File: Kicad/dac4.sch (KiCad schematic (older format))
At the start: 10 parts

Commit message: Add 4-bit Video DAC, and re-wire BMC.
Now the BMC is an SPI device, and has a four-wire UART.
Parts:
- renumbered R105 to R1401, R106 to R1402, R107 to R1403, R108 to R1404, R109 to R1405, R110 to R1406, R111 to R1407, R112 to R1408, R113 to R1409, R114 to R1410
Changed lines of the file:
@@
 Sheet 14 16
 Title "Neotron Common Hardware - 4-bit DAC"
-Date "2021-01-01"
+Date "2021-04-02"
 Rev "[Uncontrolled]"
 Comp "https://neotron-compute.github.io/"
@@
 AR Path="/5FDE658D/6009CBAC/5F5F4D05" Ref="R?"  Part="1"
 AR Path="/5FDE658D/600A04B7/5F5F4D05" Ref="R?"  Part="1"
-AR Path="/60677AF0/5FEFB226/5F5F4D05" Ref="R105"  Part="1"
-AR Path="/60677AF0/6068202E/5F5F4D05" Ref="R115"  Part="1"
-AR Path="/60677AF0/600A04B7/5F5F4D05" Ref="R125"  Part="1"
-F 0 "R125" H 3570 2746 50  0000 L CNN
+AR Path="/60677AF0/5FEFB226/5F5F4D05" Ref="R1401"  Part="1"
+AR Path="/60677AF0/6068202E/5F5F4D05" Ref="R1501"  Part="1"
+AR Path="/60677AF0/600A04B7/5F5F4D05" Ref="R1601"  Part="1"
+F 0 "R1601" H 3570 2746 50  0000 L CNN
 F 1 "24k 0.5%" H 3570 2655 50  0000 L CNN
 F 2 "Resistor_SMD:R_0805_2012Metric_Pad1.20x1.40mm_HandSolder" V 3430 2700 50  0001 C CNN
@@
 AR Path="/5FDE658D/6009CBAC/60681FF9" Ref="R?"  Part="1"
 AR Path="/5FDE658D/600A04B7/60681FF9" Ref="R?"  Part="1"
-AR Path="/60677AF0/5FEFB226/60681FF9" Ref="R107"  Part="1"
-AR Path="/60677AF0/6068202E/60681FF9" Ref="R117"  Part="1"
-AR Path="/60677AF0/600A04B7/60681FF9" Ref="R127"  Part="1"
-F 0 "R127" V 4100 3000 50  0000 C CNN
+AR Path="/60677AF0/5FEFB226/60681FF9" Ref="R1403"  Part="1"
+AR Path="/60677AF0/6068202E/60681FF9" Ref="R1503"  Part="1"
+AR Path="/60677AF0/600A04B7/60681FF9" Ref="R1603"  Part="1"
+F 0 "R1603" V 4100 3000 50  0000 C CNN
 F 1 "12k 0.5%" V 4200 3000 50  0000 C CNN
 F 2 "Resistor_SMD:R_0805_2012Metric_Pad1.20x1.40mm_HandSolder" V 3930 3000 50  0001 C CNN
@@
 AR Path="/5FDE658D/6009CBAC/60681FFA" Ref="R?"  Part="1"
 AR Path="/5FDE658D/600A04B7/60681FFA" Ref="R?"  Part="1"
-AR Path="/60677AF0/5FEFB226/60681FFA" Ref="R108"  Part="1"
-AR Path="/60677AF0/6068202E/60681FFA" Ref="R118"  Part="1"
-AR Path="/60677AF0/600A04B7/60681FFA" Ref="R128"  Part="1"
-F 0 "R128" H 4570 2746 50  0000 L CNN
+AR Path="/60677AF0/5FEFB226/60681FFA" Ref="R1404"  Part="1"
+AR Path="/60677AF0/6068202E/60681FFA" Ref="R1504"  Part="1"
+AR Path="/60677AF0/600A04B7/60681FFA" Ref="R1604"  Part="1"
+F 0 "R1604" H 4570 2746 50  0000 L CNN
 F 1 "24k 0.5%" H 4570 2655 50  0000 L CNN
 F 2 "Resistor_SMD:R_0805_2012Metric_Pad1.20x1.40mm_HandSolder" V 4430 2700 50  0001 C CNN
@@
 AR Path="/5FDE658D/6009CBAC/60681FFB" Ref="R?"  Part="1"
 AR Path="/5FDE658D/600A04B7/60681FFB" Ref="R?"  Part="1"
-AR Path="/60677AF0/5FEFB226/60681FFB" Ref="R109"  Part="1"
-AR Path="/60677AF0/6068202E/60681FFB" Ref="R119"  Part="1"
-AR Path="/60677AF0/600A04B7/60681FFB" Ref="R129"  Part="1"
-F 0 "R129" V 5100 3000 50  0000 C CNN
+AR Path="/60677AF0/5FEFB226/60681FFB" Ref="R1405"  Part="1"
+AR Path="/60677AF0/6068202E/60681FFB" Ref="R1505"  Part="1"
+AR Path="/60677AF0/600A04B7/60681FFB" Ref="R1605"  Part="1"
+F 0 "R1605" V 5100 3000 50  0000 C CNN
 F 1 "12k 0.5%" V 5200 3000 50  0000 C CNN
 F 2 "Resistor_SMD:R_0805_2012Metric_Pad1.20x1.40mm_HandSolder" V 4930 3000 50  0001 C CNN
@@
 AR Path="/5FDE658D/6009CBAC/60681FFC" Ref="R?"  Part="1"
 AR Path="/5FDE658D/600A04B7/60681FFC" Ref="R?"  Part="1"
-AR Path="/60677AF0/5FEFB226/60681FFC" Ref="R111"  Part="1"
-AR Path="/60677AF0/6068202E/60681FFC" Ref="R121"  Part="1"
-AR Path="/60677AF0/600A04B7/60681FFC" Ref="R131"  Part="1"
-F 0 "R131" V 6100 3000 50  0000 C CNN
+AR Path="/60677AF0/5FEFB226/60681FFC" Ref="R1407"  Part="1"
+AR Path="/60677AF0/6068202E/60681FFC" Ref="R1507"  Part="1"
+AR Path="/60677AF0/600A04B7/60681FFC" Ref="R1607"  Part="1"
+F 0 "R1607" V 6100 3000 50  0000 C CNN
 F 1 "12k 0.5%" V 6200 3000 50  0000 C CNN
 F 2 "Resistor_SMD:R_0805_2012Metric_Pad1.20x1.40mm_HandSolder" V 5930 3000 50  0001 C CNN
@@
 AR Path="/5FDE658D/6009CBAC/60681FFD" Ref="R?"  Part="1"
 AR Path="/5FDE658D/600A04B7/60681FFD" Ref="R?"  Part="1"
-AR Path="/60677AF0/5FEFB226/60681FFD" Ref="R113"  Part="1"
-AR Path="/60677AF0/6068202E/60681FFD" Ref="R123"  Part="1"
-AR Path="/60677AF0/600A04B7/60681FFD" Ref="R133"  Part="1"
-F 0 "R133" V 7100 3000 50  0000 C CNN
+AR Path="/60677AF0/5FEFB226/60681FFD" Ref="R1409"  Part="1"
+AR Path="/60677AF0/6068202E/60681FFD" Ref="R1509"  Part="1"
+AR Path="/60677AF0/600A04B7/60681FFD" Ref="R1609"  Part="1"
+F 0 "R1609" V 7100 3000 50  0000 C CNN
 F 1 "12k 0.5%" V 7200 3000 50  0000 C CNN
 F 2 "Resistor_SMD:R_0805_2012Metric_Pad1.20x1.40mm_HandSolder" V 6930 3000 50  0001 C CNN
@@
 AR Path="/5FDE658D/6009CBAC/60681FFF" Ref="R?"  Part="1"
 AR Path="/5FDE658D/600A04B7/60681FFF" Ref="R?"  Part="1"
-AR Path="/60677AF0/5FEFB226/60681FFF" Ref="R114"  Part="1"
-AR Path="/60677AF0/6068202E/60681FFF" Ref="R124"  Part="1"
-AR Path="/60677AF0/600A04B7/60681FFF" Ref="R134"  Part="1"
-F 0 "R134" H 7620 3346 50  0000 L CNN
+AR Path="/60677AF0/5FEFB226/60681FFF" Ref="R1410"  Part="1"
+AR Path="/60677AF0/6068202E/60681FFF" Ref="R1510"  Part="1"
+AR Path="/60677AF0/600A04B7/60681FFF" Ref="R1610"  Part="1"
+F 0 "R1610" H 7620 3346 50  0000 L CNN
 F 1 "3480 0.5%" H 7620 3255 50  0000 L CNN
 F 2 "Resistor_SMD:R_0805_2012Metric_Pad1.20x1.40mm_HandSolder" V 7480 3300 50  0001 C CNN
@@
 AR Path="/5FDE658D/6009CBAC/60682000" Ref="#PWR?"  Part="1"
 AR Path="/5FDE658D/600A04B7/60682000" Ref="#PWR?"  Part="1"
-AR Path="/60677AF0/5FEFB226/60682000" Ref="#PWR0224"  Part="1"
-AR Path="/60677AF0/6068202E/60682000" Ref="#PWR0226"  Part="1"
-AR Path="/60677AF0/600A04B7/60682000" Ref="#PWR0228"  Part="1"
-F 0 "#PWR0228" H 3500 3350 50  0001 C CNN
+AR Path="/60677AF0/5FEFB226/60682000" Ref="#PWR01401"  Part="1"
+AR Path="/60677AF0/6068202E/60682000" Ref="#PWR01501"  Part="1"
+AR Path="/60677AF0/600A04B7/60682000" Ref="#PWR01601"  Part="1"
+F 0 "#PWR01601" H 3500 3350 50  0001 C CNN
 F 1 "GND" H 3505 3427 50  0000 C CNN
 F 2 "" H 3500 3600 50  0001 C CNN
@@
 AR Path="/5FDE658D/6009CBAC/60682001" Ref="#PWR?"  Part="1"
 AR Path="/5FDE658D/600A04B7/60682001" Ref="#PWR?"  Part="1"
-AR Path="/60677AF0/5FEFB226/60682001" Ref="#PWR0225"  Part="1"
-AR Path="/60677AF0/6068202E/60682001" Ref="#PWR0227"  Part="1"
-AR Path="/60677AF0/600A04B7/60682001" Ref="#PWR0229"  Part="1"
-F 0 "#PWR0229" H 7550 3350 50  0001 C CNN
+AR Path="/60677AF0/5FEFB226/60682001" Ref="#PWR01402"  Part="1"
+AR Path="/60677AF0/6068202E/60682001" Ref="#PWR01502"  Part="1"
+AR Path="/60677AF0/600A04B7/60682001" Ref="#PWR01602"  Part="1"
+F 0 "#PWR01602" H 7550 3350 50  0001 C CNN
 F 1 "GND" H 7555 3427 50  0000 C CNN
 F 2 "" H 7550 3600 50  0001 C CNN
@@
 AR Path="/5FDE658D/6009CBAC/60682002" Ref="R?"  Part="1"
 AR Path="/5FDE658D/600A04B7/60682002" Ref="R?"  Part="1"
-AR Path="/60677AF0/5FEFB226/60682002" Ref="R106"  Part="1"
-AR Path="/60677AF0/6068202E/60682002" Ref="R116"  Part="1"
-AR Path="/60677AF0/600A04B7/60682002" Ref="R126"  Part="1"
-F 0 "R126" H 3570 3346 50  0000 L CNN
+AR Path="/60677AF0/5FEFB226/60682002" Ref="R1402"  Part="1"
+AR Path="/60677AF0/6068202E/60682002" Ref="R1502"  Part="1"
+AR Path="/60677AF0/600A04B7/60682002" Ref="R1602"  Part="1"
+F 0 "R1602" H 3570 3346 50  0000 L CNN
 F 1 "24k 0.5%" H 3570 3255 50  0000 L CNN
 F 2 "Resistor_SMD:R_0805_2012Metric_Pad1.20x1.40mm_HandSolder" V 3430 3300 50  0001 C CNN
@@
 AR Path="/5FDE658D/6009CBAC/60682003" Ref="R?"  Part="1"
 AR Path="/5FDE658D/600A04B7/60682003" Ref="R?"  Part="1"
-AR Path="/60677AF0/5FEFB226/60682003" Ref="R110"  Part="1"
-AR Path="/60677AF0/6068202E/60682003" Ref="R120"  Part="1"
-AR Path="/60677AF0/600A04B7/60682003" Ref="R130"  Part="1"
-F 0 "R130" H 5570 2746 50  0000 L CNN
+AR Path="/60677AF0/5FEFB226/60682003" Ref="R1406"  Part="1"
+AR Path="/60677AF0/6068202E/60682003" Ref="R1506"  Part="1"
+AR Path="/60677AF0/600A04B7/60682003" Ref="R1606"  Part="1"
+F 0 "R1606" H 5570 2746 50  0000 L CNN
 F 1 "24k 0.5%" H 5570 2655 50  0000 L CNN
 F 2 "Resistor_SMD:R_0805_2012Metric_Pad1.20x1.40mm_HandSolder" V 5430 2700 50  0001 C CNN
@@
 AR Path="/5FDE658D/6009CBAC/5F5FD329" Ref="R?"  Part="1"
 AR Path="/5FDE658D/600A04B7/5F5FD329" Ref="R?"  Part="1"
-AR Path="/60677AF0/5FEFB226/5F5FD329" Ref="R112"  Part="1"
-AR Path="/60677AF0/6068202E/5F5FD329" Ref="R122"  Part="1"
-AR Path="/60677AF0/600A04B7/5F5FD329" Ref="R132"  Part="1"
-F 0 "R132" H 6570 2746 50  0000 L CNN
+AR Path="/60677AF0/5FEFB226/5F5FD329" Ref="R1408"  Part="1"
+AR Path="/60677AF0/6068202E/5F5FD329" Ref="R1508"  Part="1"
+AR Path="/60677AF0/600A04B7/5F5FD329" Ref="R1608"  Part="1"
+F 0 "R1608" H 6570 2746 50  0000 L CNN
 F 1 "24k 0.5%" H 6570 2655 50  0000 L CNN
 F 2 "Resistor_SMD:R_0805_2012Metric_Pad1.20x1.40mm_HandSolder" V 6430 2700 50  0001 C CNN

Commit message: Tidy up part nos and swapped I2C/UART on BMC.
Mark all resistors as 1% if not specified.
Added some Mouser part numbers.
BMC can now be programmed over UART.
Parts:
- R1410: Digikey RMCF0805FG3K30-ND -> RNCF0805DTE3K48CT-ND; MPN RMCF0805FG3K30 -> RNCF0805DTE3K48
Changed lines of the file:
@@
 F 3 "~" H 7550 3300 50  0001 C CNN
 F 4 "0" H 7550 3300 50  0001 C CNN "DNP"
-F 5 "RMCF0805FG3K30-ND" H 7550 3300 50  0001 C CNN "Digikey"
-F 6 "RMCF0805FG3K30" H 7550 3300 50  0001 C CNN "MPN"
+F 5 "RNCF0805DTE3K48CT-ND" H 7550 3300 50  0001 C CNN "Digikey"
+F 6 "RNCF0805DTE3K48" H 7550 3300 50  0001 C CNN "MPN"
 F 7 "Stackpole" H 7550 3300 50  0001 C CNN "Manufacturer"
 	1    7550 3300

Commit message: Changes to BMC
* Swapped BUTTON_PWR and SYS_RESET to avoid DRC issue
* Split PSU and BMC into two separate sheets
* Swapped some pins on the STM32 to make it compatible with more
alternatives
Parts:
- renumbered R1401 to R1301, R1402 to R1302, R1403 to R1303, R1404 to R1304, R1405 to R1305, R1406 to R1306, R1407 to R1307, R1408 to R1308, R1409 to R1309, R1410 to R1310

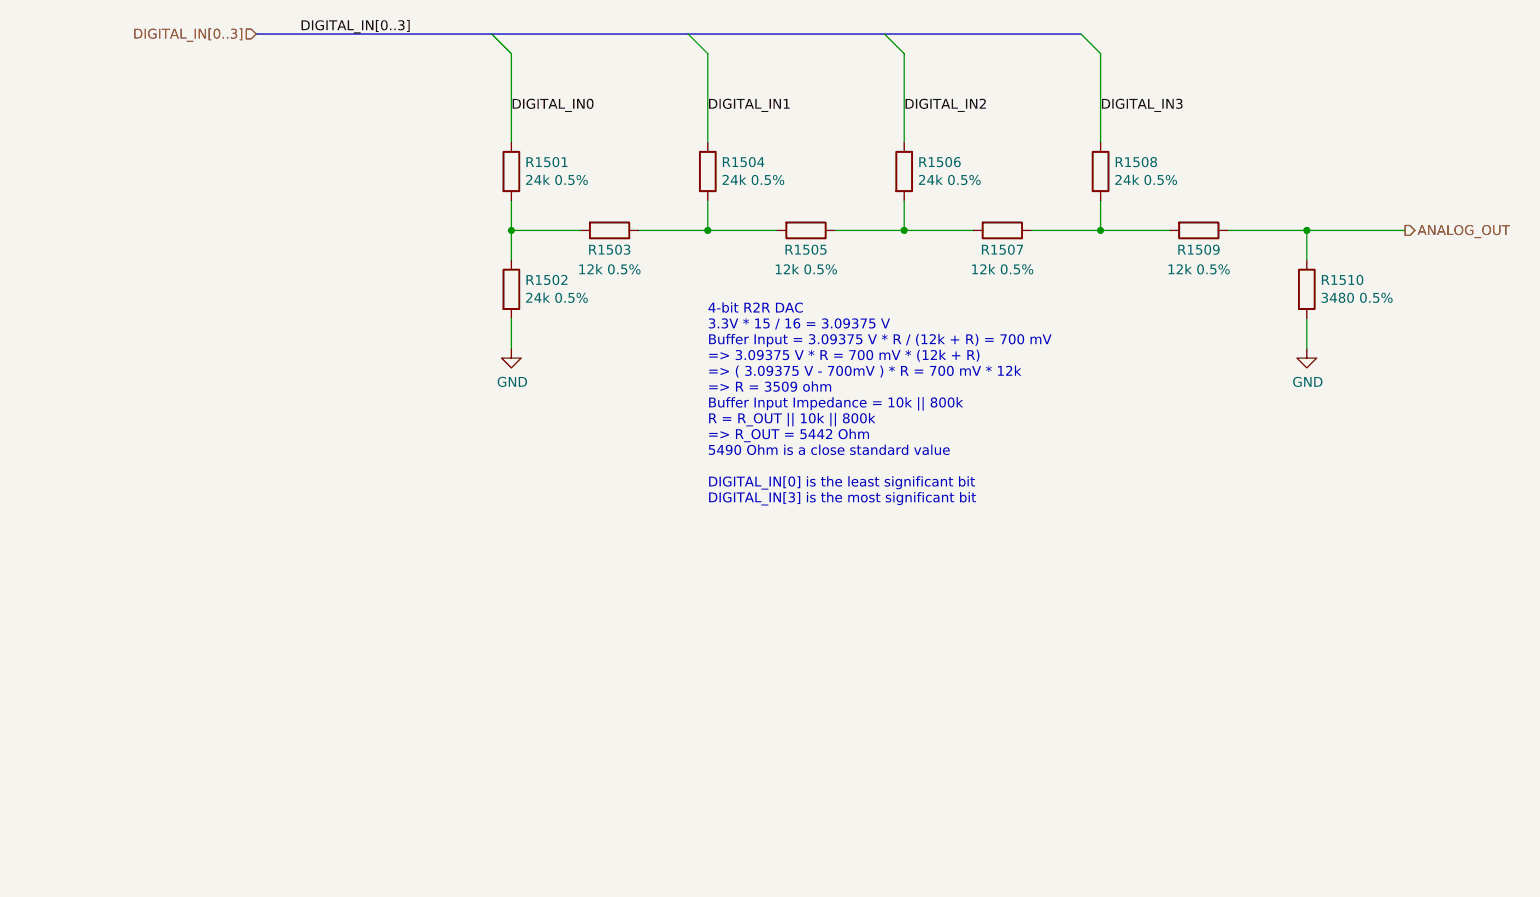
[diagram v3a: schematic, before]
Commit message: Brought in sheets from Neotron Pico.
Also includes DB15HD and PSU 3D models.
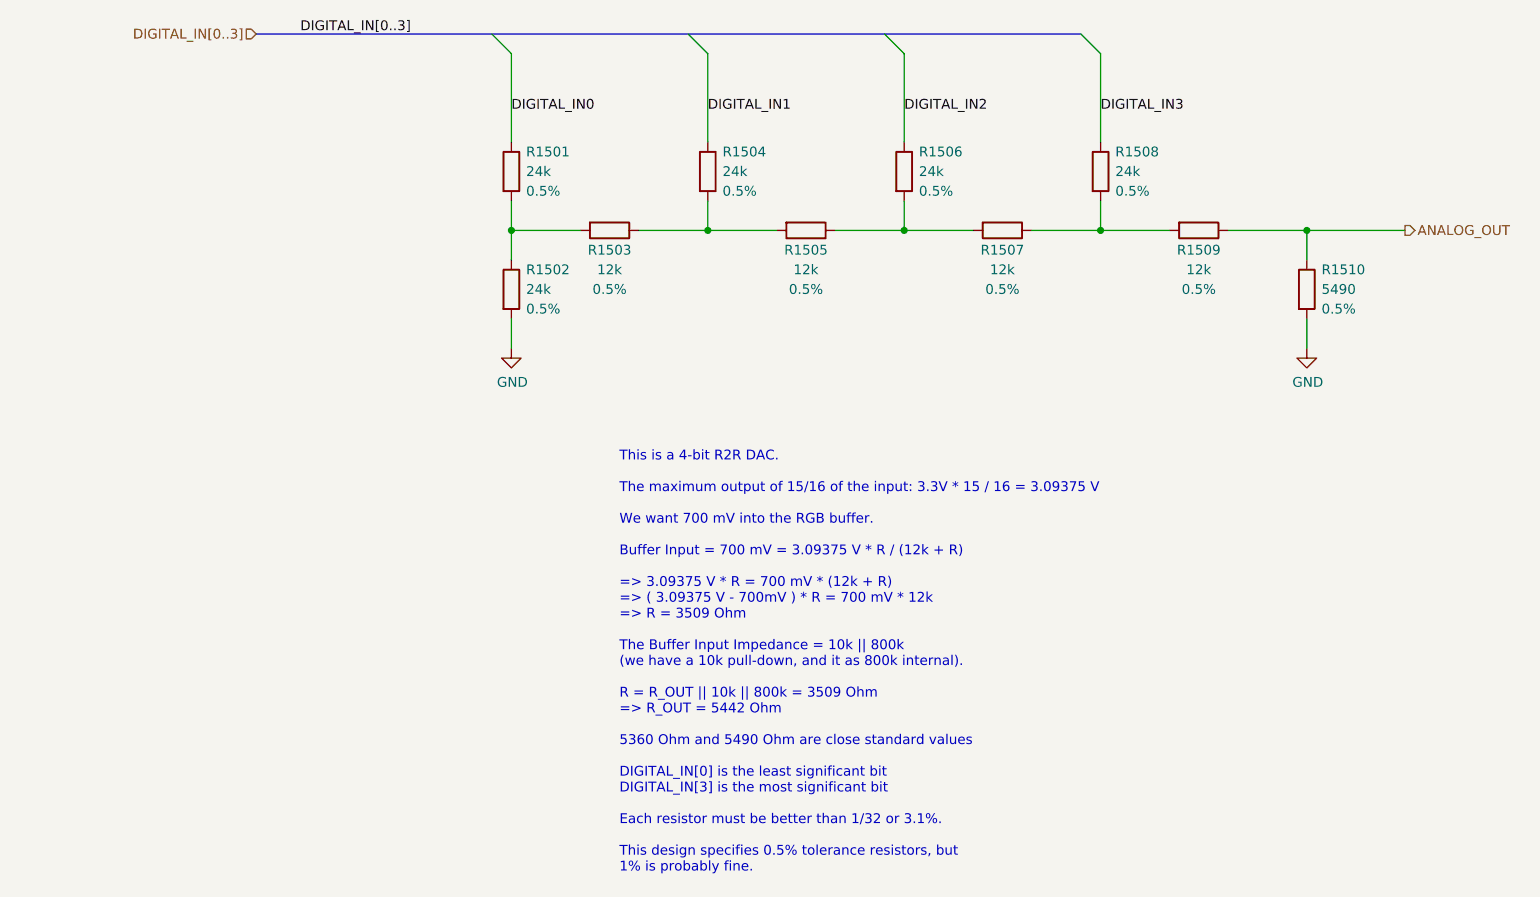
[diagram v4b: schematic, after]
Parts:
- R1301, R1302, R1304, R1306, R1308: value 24k 0.5% -> 24k; LCSC Part# (none) -> C17575; Tolerance (none) -> 0.5%
- R1303, R1305, R1307, R1309: value 12k 0.5% -> 12k; LCSC Part# (none) -> C97163; Tolerance (none) -> 0.5%
- R1310: value 3480 0.5% -> 5490; Digikey RNCF0805DTE3K48CT-ND -> RNCF0805DTE5K49CT-ND; LCSC Part# (none) -> C17726; MPN RNCF0805DTE3K48 -> RNCF0805DTE5K49; Tolerance (none) -> 0.5%
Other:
- note added: "This is a 4-bit R2R DAC.\n\nThe maximum output of 15/16 of the input: 3.3V * 15 / 16 = 3.09375 V\n\nWe want 700 mV into the RGB buffer.\n\nBuffer Input = 700 mV = 3.09375 V * R / (12k + R)\n\n=> 3.09375 V * R = 700 mV * (12k + R)\n=> ( 3.09375 V - 700mV ) * R = 700 mV * 12k\n=> R = 3509 Ohm\n\nThe Buffer Input Impedance = 10k || 800k\n(we have a 10k pull-down, and it as 800k internal).\n\nR = R_O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"
- note removed: "4-bit R2R DAC\n3.3V * 15 / 16 = 3.09375 V\nBuffer Input = 3.09375 V * R / (12k + R) = 700 mV\n=> 3.09375 V * R = 700 mV * (12k + R)\n=> ( 3.09375 V - 700mV ) * R = 700 mV * 12k\n=> R = 3509 ohm\nBuffer Input Impedance = 10k || 800k\nR = R_OUT || 10k || 800k\n=> R_OUT = 5442 Ohm\n5490 Ohm is a close standard value\n\nDIGITAL_IN[0] is the least significant bit\nDIGITAL_IN[3] is the most significant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"

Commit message: Merge in more changes.
Mostly lowering voltage tolerances to minimum required.
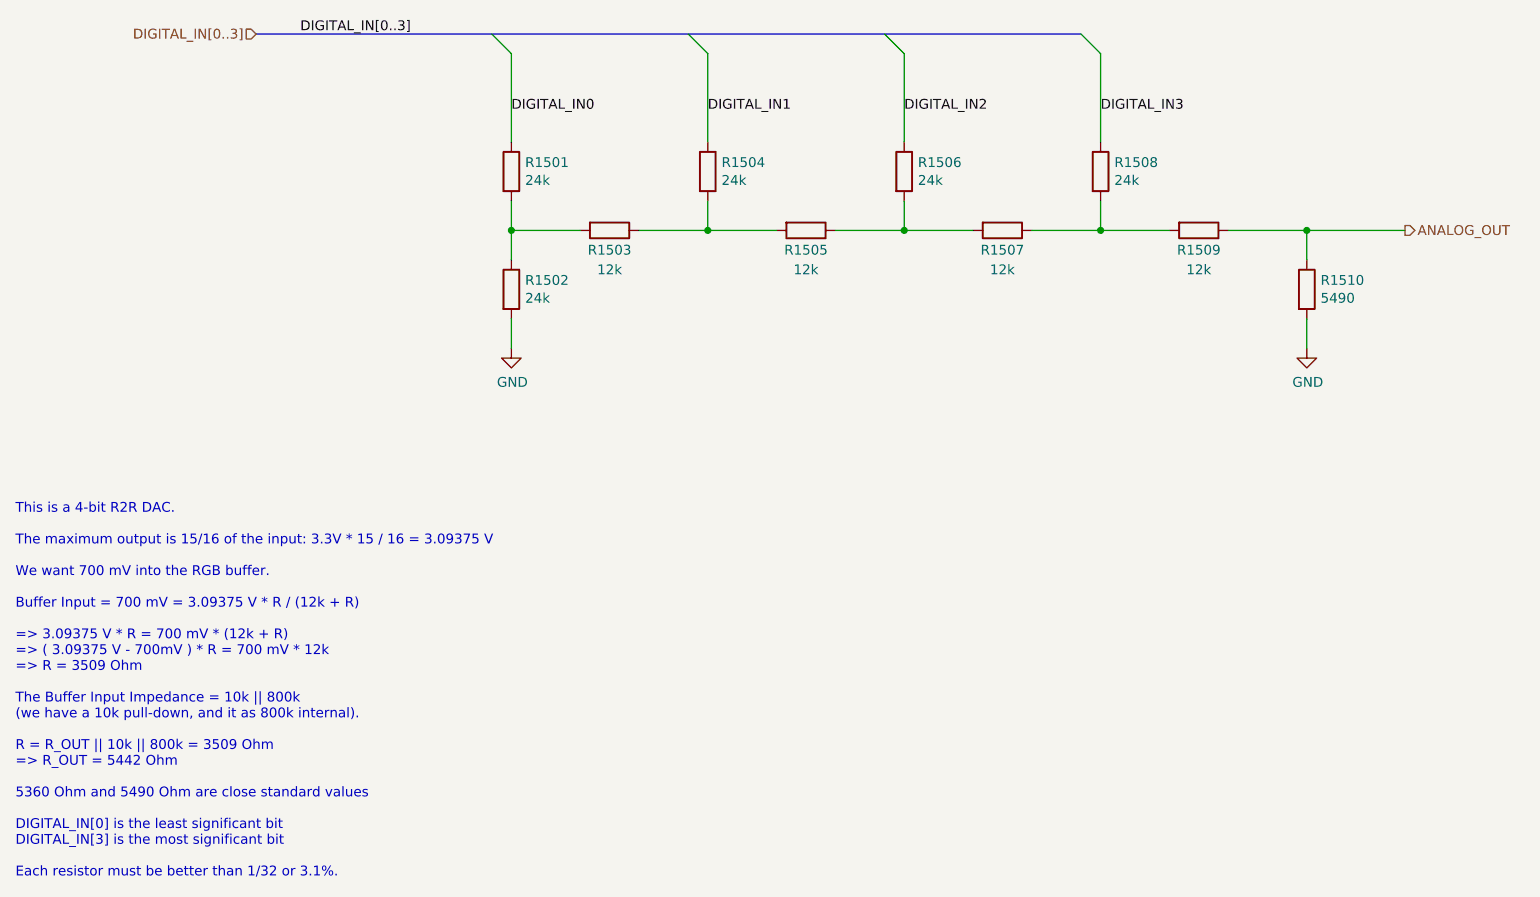
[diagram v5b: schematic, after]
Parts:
- R1301, R1302, R1304, R1306, R1308: MPN RNCF0805DTE24K0 -> RMCF0805FT24K0; Tolerance 0.5% -> 1%
- R1303, R1305, R1307, R1309: MPN RNCF0805DTE12K0 -> RMCF0805FT12K0; Tolerance 0.5% -> 1%
- R1310: LCSC Part# C17726 -> C79483; MPN RNCF0805DTE5K49 -> RMCF0805FT5K49; Tolerance 0.5% -> 1%
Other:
- note added: "This is a 4-bit R2R DAC.\n\nThe maximum output is 15/16 of the input: 3.3V * 15 / 16 = 3.09375 V\n\nWe want 700 mV into the RGB buffer.\n\nBuffer Input = 700 mV = 3.09375 V * R / (12k + R)\n\n=> 3.09375 V * R = 700 mV * (12k + R)\n=> ( 3.09375 V - 700mV ) * R = 700 mV * 12k\n=> R = 3509 Ohm\n\nThe Buffer Input Impedance = 10k || 800k\n(we have a 10k pull-down, and it as 800k internal).\n\nR = R_O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"
- note removed: "This is a 4-bit R2R DAC.\n\nThe maximum output of 15/16 of the input: 3.3V * 15 / 16 = 3.09375 V\n\nWe want 700 mV into the RGB buffer.\n\nBuffer Input = 700 mV = 3.09375 V * R / (12k + R)\n\n=> 3.09375 V * R = 700 mV * (12k + R)\n=> ( 3.09375 V - 700mV ) * R = 700 mV * 12k\n=> R = 3509 Ohm\n\nThe Buffer Input Impedance = 10k || 800k\n(we have a 10k pull-down, and it as 800k internal).\n\nR = R_O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"
